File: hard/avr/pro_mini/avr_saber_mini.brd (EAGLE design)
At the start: 83.5 x 34.3 mm, 32 parts, among them U3 USD-SOCKETUSD

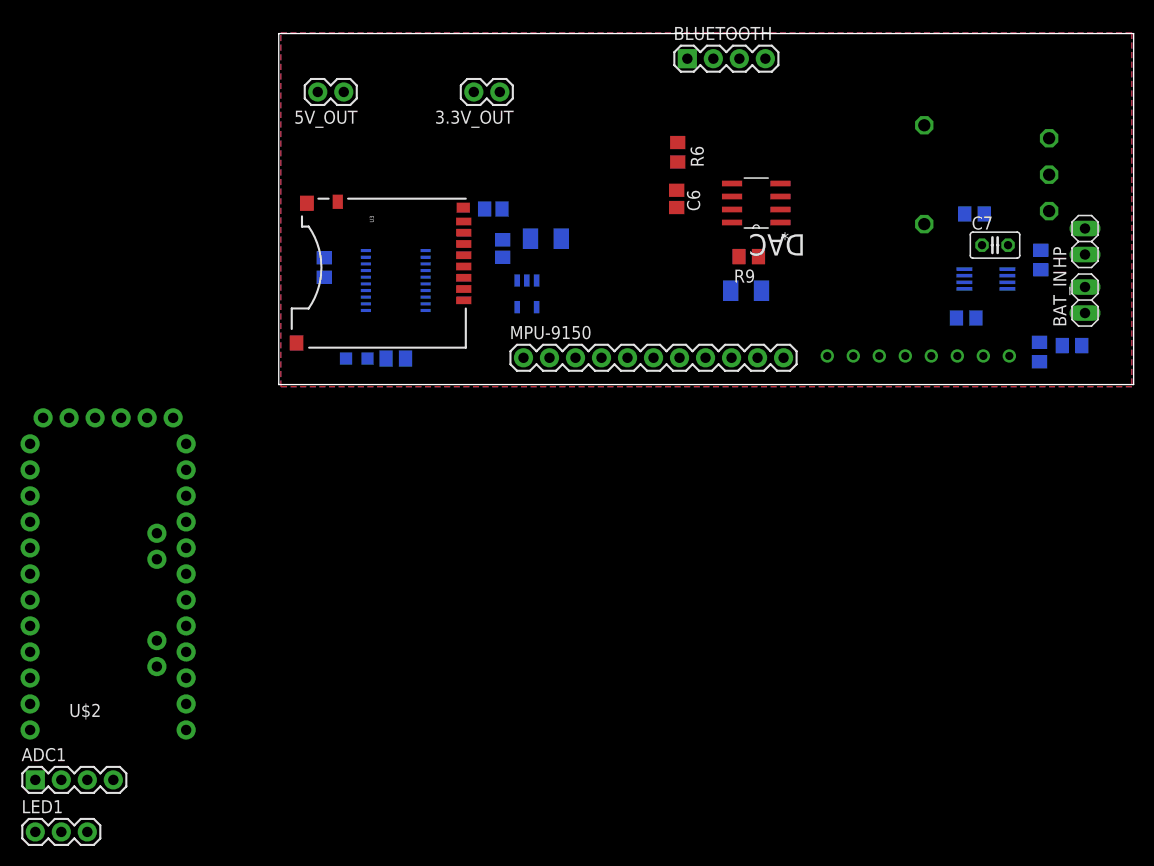
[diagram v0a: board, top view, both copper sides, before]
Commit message: new card with mini pro
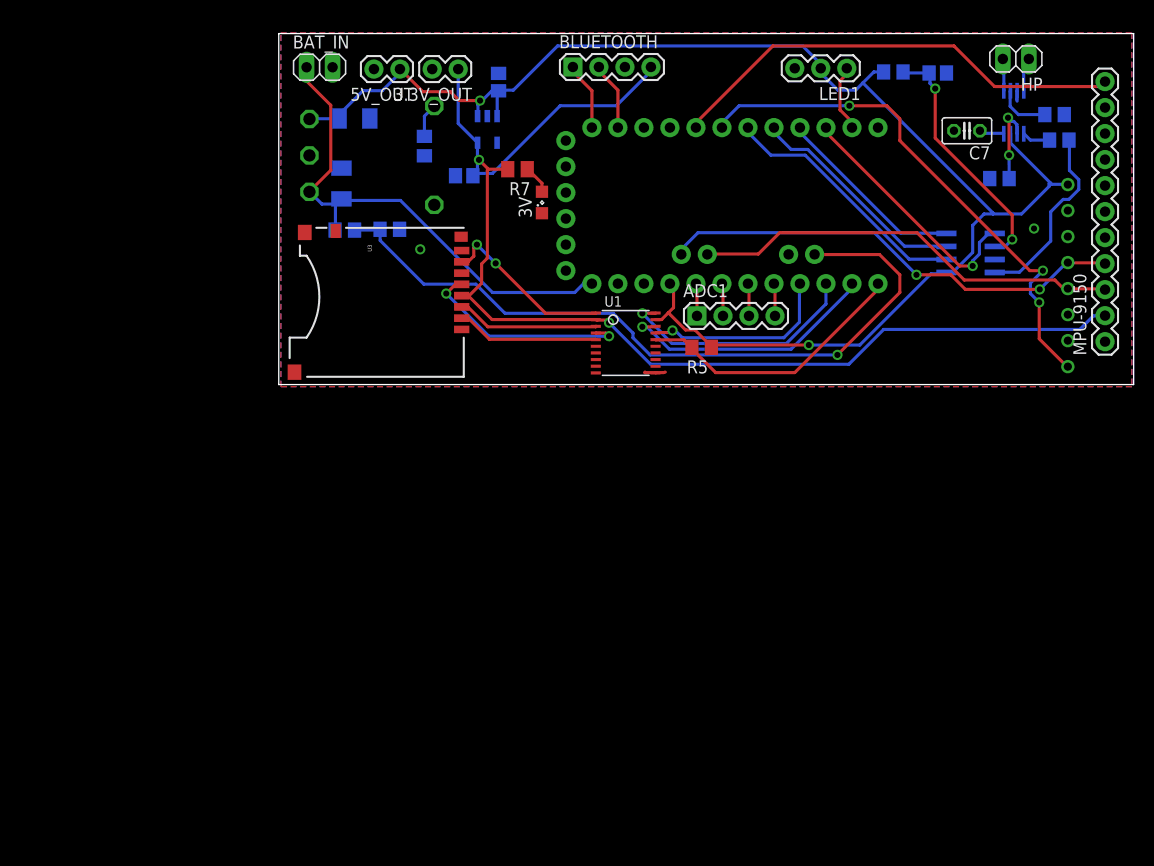
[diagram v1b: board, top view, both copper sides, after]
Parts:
- moved LED1 108.8 mm to (55.5, 30.9), turned to 180 degrees
- moved ADC1 78.9 mm to (40.8, 6.71)
- moved BAT_IN 78.1 mm to (3.99, 31.0), turned to 0 degrees
- moved U$4 72.4 mm to (3.00, 18.8), turned to 180 degrees
- moved R2 71.9 mm to (6.45, 15.1), turned to 0 degrees
- moved U$2 69.9 mm to (43.3, 17.5), flipped to the bottom, turned to 270 degrees
- moved R3 64.6 mm to (10.8, 15.2), turned to 0 degrees
- moved MPU-9150 56.8 mm to (80.7, 4.19), turned to 90 degrees
- moved R4 54.1 mm to (14.2, 23.3), turned to 90 degrees
- moved C5 41.8 mm to (7.39, 26.0), turned to 180 degrees
- moved R5 37.7 mm to (41.3, 3.63), flipped to the top, turned to 180 degrees
- moved R9 32.4 mm to (76.2, 23.9), flipped to the bottom
- moved C6 28.3 mm to (64.4, 30.4), flipped to the bottom, turned to 180 degrees
- moved 3V 23.6 mm to (25.7, 17.8), flipped to the top, turned to 90 degrees
- moved U1 23.3 mm to (33.9, 4.06), flipped to the top
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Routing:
- net +5V: track 0.00 -> 147.4 mm, vias 0 -> 2
- net +3V3: track 0.00 -> 117.5 mm, vias 0 -> 2
- net BATTLEVEL: track 0.00 -> 72.7 mm, vias 0 -> 1
- net INT1: track 0.00 -> 51.9 mm, vias 0 -> 3
- net +12V: track 0.00 -> 49.8 mm
- net SCL: track 0.00 -> 46.0 mm, vias 0 -> 2
- net INT0: track 0.00 -> 45.4 mm
- net SDA: track 0.00 -> 42.1 mm
- net MMC_CS: track 0.00 -> 27.1 mm
- net MOSI: track 0.00 -> 25.6 mm, vias 0 -> 1
- net DAC_CS: track 0.00 -> 25.0 mm
- net DAC_LATCH: track 0.00 -> 24.6 mm, vias 0 -> 1
- net N$19: track 0.00 -> 24.2 mm, vias 0 -> 2
- net MISO: track 0.00 -> 24.1 mm, vias 0 -> 1
- net DAC_SCK: track 0.00 -> 21.9 mm
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
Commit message: new version
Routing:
- net +3V3: track 117.5 -> 127.3 mm, vias 2 -> 1
- net N$6: track 20.9 -> 29.4 mm, vias 2 -> 0
- net MOSI: track 25.6 -> 33.3 mm
- net GND: track 3.12 -> 5.15 mm, vias 2 -> 5
- net MISO: track 24.1 -> 22.5 mm
- net MMC_CS: track 27.1 -> 26.4 mm
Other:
- board text added: "3V3"
- board text added: "5V"
- board text added: "ACC Centrale"
- board text added: "AOP Audio"
- board text added: "BAT"
- board text added: "DAC"
- board text added: "HP"
- board text added: "LED"
- board text added: "PTH08080"
- board text added: "arduino mini pro"
- board text added: "bluetooth"
